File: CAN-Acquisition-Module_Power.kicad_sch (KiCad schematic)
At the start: 8 parts

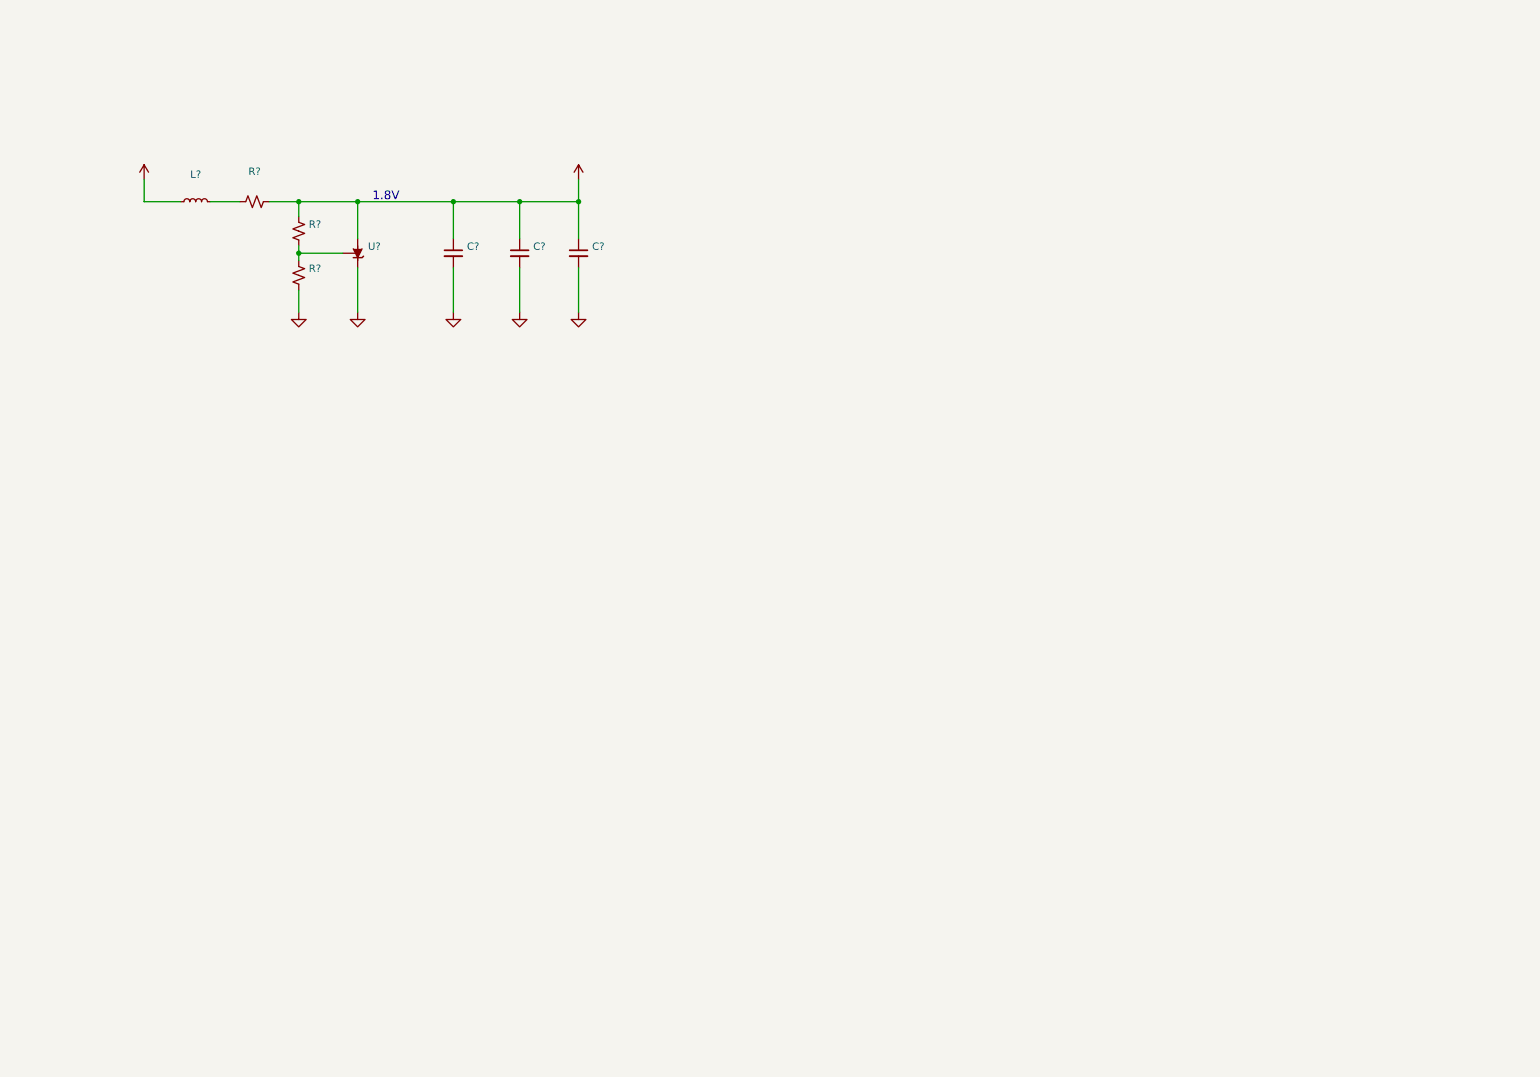
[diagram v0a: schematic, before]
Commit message: Added CAN page
also power section has advanced
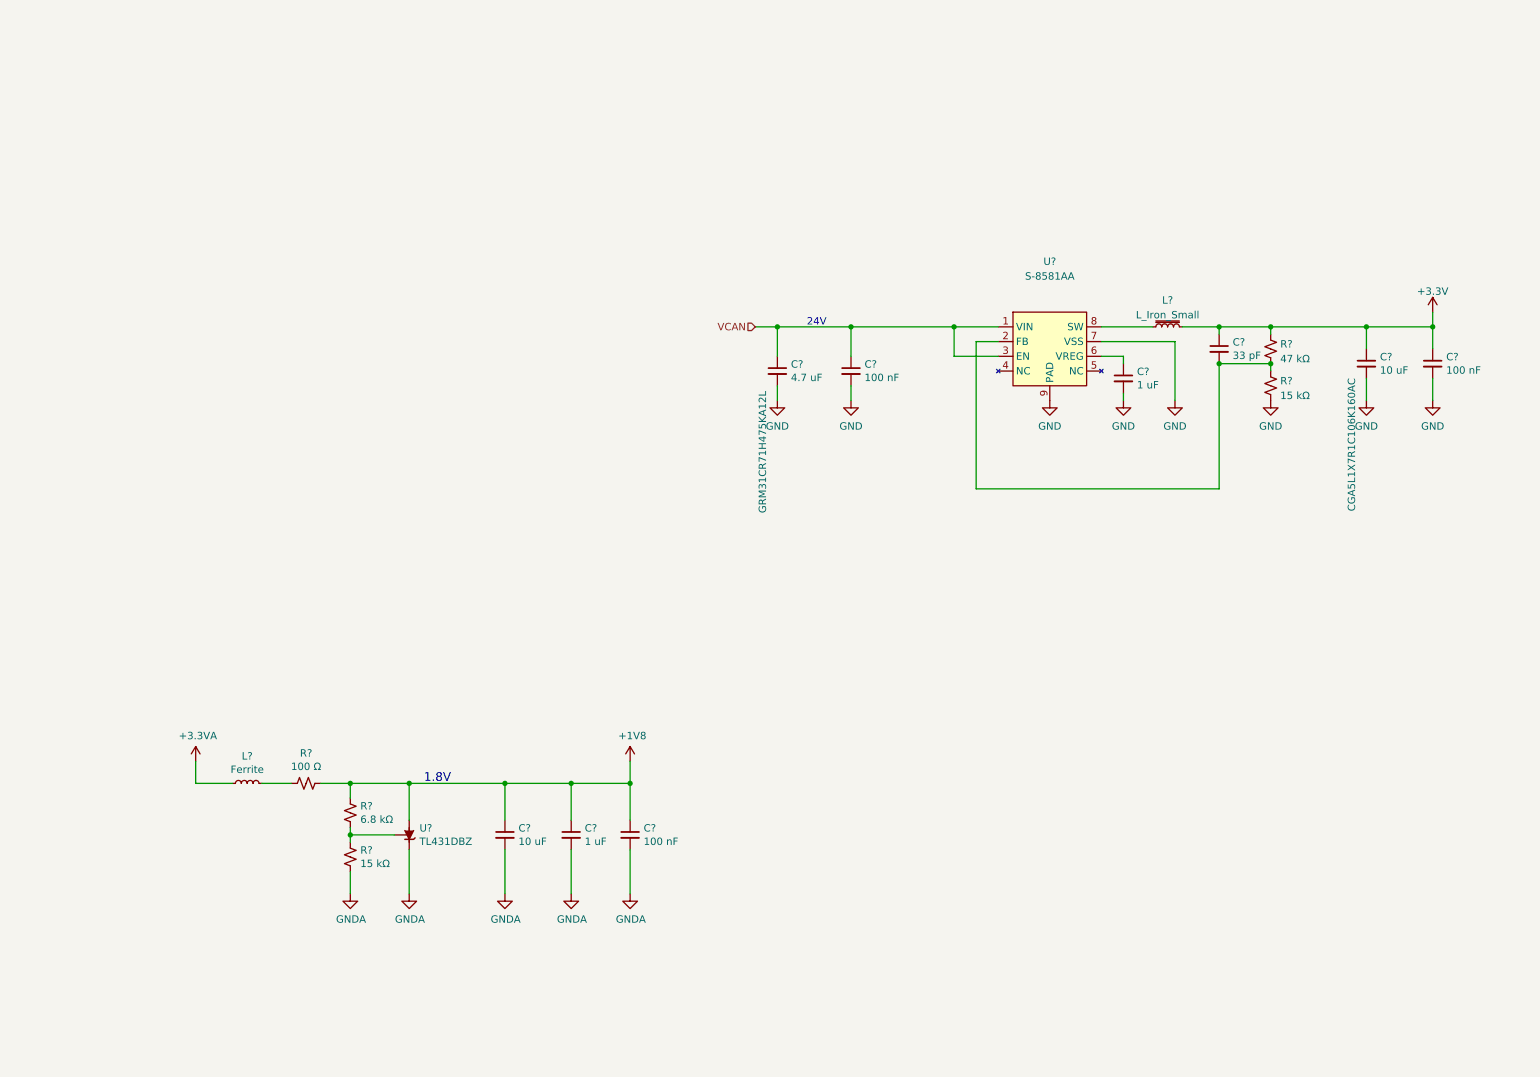
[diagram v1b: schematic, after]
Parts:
- added C?: 100 nF, Capacitor_SMD:C_0402_1005Metric, symbol Device:C_Small
- added C?: 100 nF, Capacitor_SMD:C_0603_1608Metric, symbol Device:C_Small
- added C?: 33 pF, Capacitor_SMD:C_0603_1608Metric, symbol Device:C_Small
- added C?: 10 uF, Capacitor_SMD:C_1206_3216Metric, symbol Device:C_Small
- added C?: 1 uF, Capacitor_SMD:C_0603_1608Metric, symbol Device:C_Small
- added C?: 4.7 uF, Capacitor_SMD:C_1206_3216Metric, symbol Device:C_Small
- added L?: L_Iron_Small, Inductor_SMD:L_1008_2520Metric, symbol Device:L_Iron_Small
- added R?: 15 kΩ, Resistor_SMD:R_0603_1608Metric, symbol Device:R_Small_US
- added R?: 47 kΩ, Resistor_SMD:R_0603_1608Metric, symbol Device:R_Small_US
- added U?: S-8581AA, CAN-Acquisition-Module:Ablic_HSTN-8-A, symbol CAN-Acquisition-Module:S-8581AA
- C?: value (none) -> 10 uF; footprint (none) -> Capacitor_SMD:C_1206_3216Metric
- C?: value (none) -> 1 uF; footprint (none) -> Capacitor_SMD:C_0603_1608Metric
- C?: value (none) -> 100 nF; footprint (none) -> Capacitor_SMD:C_0402_1005Metric
- L?: value (none) -> Ferrite; footprint (none) -> Inductor_SMD:L_0603_1608Metric
- R?: value (none) -> 6.8 kΩ; footprint (none) -> Resistor_SMD:R_0603_1608Metric
- R?: value (none) -> 15 kΩ; footprint (none) -> Resistor_SMD:R_0603_1608Metric
- R?: value (none) -> 100 Ω; footprint (none) -> Resistor_SMD:R_0805_2012Metric
- U?: value (none) -> TL431DBZ; footprint (none) -> Package_TO_SOT_SMD:SOT-23
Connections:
- new net: C?.2, R?.1, R?.2, U?.2 (FB)
- new net: C?.1, U?.6 (VREG)
- new net: L?.1, U?.8 (SW)
- new net +3V3: C?.1, C?.1, C?.1, L?.2, R?.1
- new net GND: C?.2, C?.2, C?.2, C?.2, C?.2, R?.2, U?.7 (VSS), U?.9 (PAD)
- new net VCAN: C?.1, C?.1, U?.1 (VIN), U?.3 (EN)
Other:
- note added: "24V"
- moved on the sheet: C?, L?, R?, U?

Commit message: Mid-day backup
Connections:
- net VCAN: no longer names the net of C?.1, C?.1, U?.1 (VIN), U?.3 (EN)
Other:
- note added: "5 to 24V"
- note removed: "24V"
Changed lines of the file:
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@@
   (junction (at 236.22 73.66) (diameter 0) (color 0 0 0 0)
-  )
-  (junction (at 151.13 67.31) (diameter 0) (color 0 0 0 0)
   )
   (junction (at 264.16 67.31) (diameter 0) (color 0 0 0 0)
@@
   )
   (wire (pts (xy 264.16 67.31) (xy 252.73 67.31))
-    (stroke (width 0) (type default) (color 0 0 0 0))
-  )
-  (wire (pts (xy 147.32 67.31) (xy 151.13 67.31))
     (stroke (width 0) (type default) (color 0 0 0 0))
   )
@@
     (stroke (width 0) (type default) (color 0 0 0 0))
   )
-  (text "24V" (at 156.21 67.31 0)
+  (text "5 to 24V" (at 156.21 67.31 0)
     (effects (font (size 1.27 1.27)) (justify left bottom))
   )
@@
     (effects (font (size 1.4986 1.4986)) (justify left bottom))
   )
-  (hierarchical_label "VCAN" (shape input) (at 147.32 67.31 180)
+  (hierarchical_label "V_CAN" (shape input) (at 88.9 67.31 180)
     (effects (font (size 1.27 1.27)) (justify right))
   )
+  (hierarchical_label "V_USB" (shape input) (at 88.9 38.1 180)
+    (effects (font (size 1.27 1.27)) (justify right))
+  )

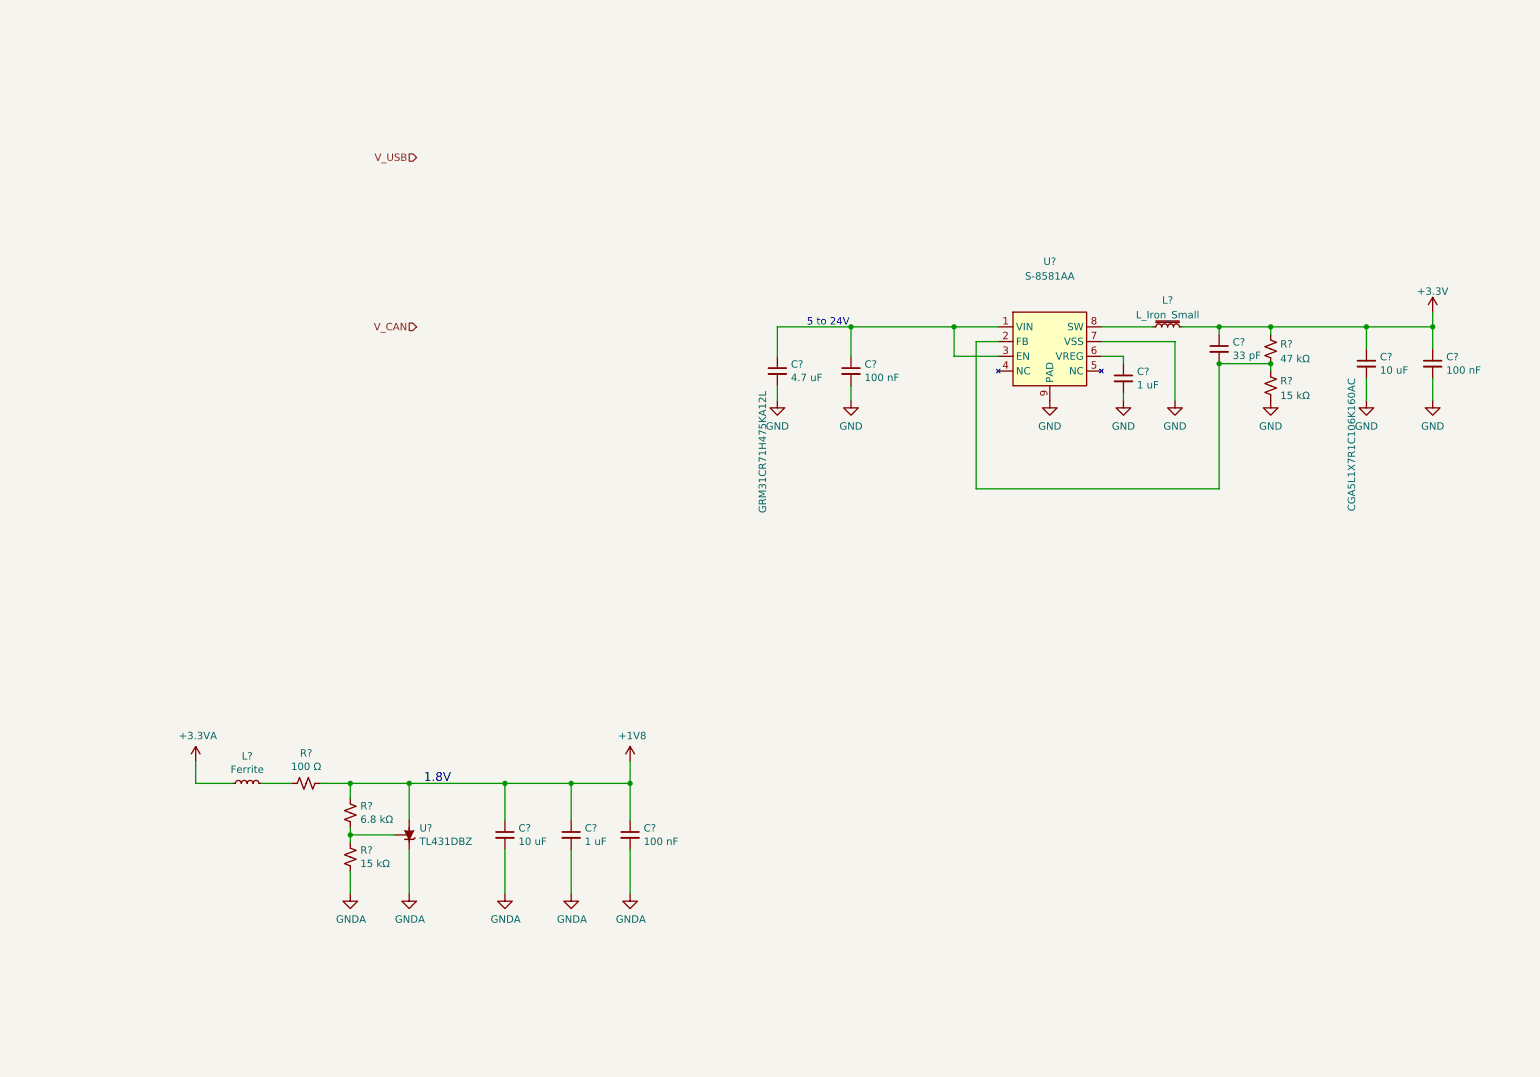
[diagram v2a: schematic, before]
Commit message: Advanced CAN section and "finished" power section
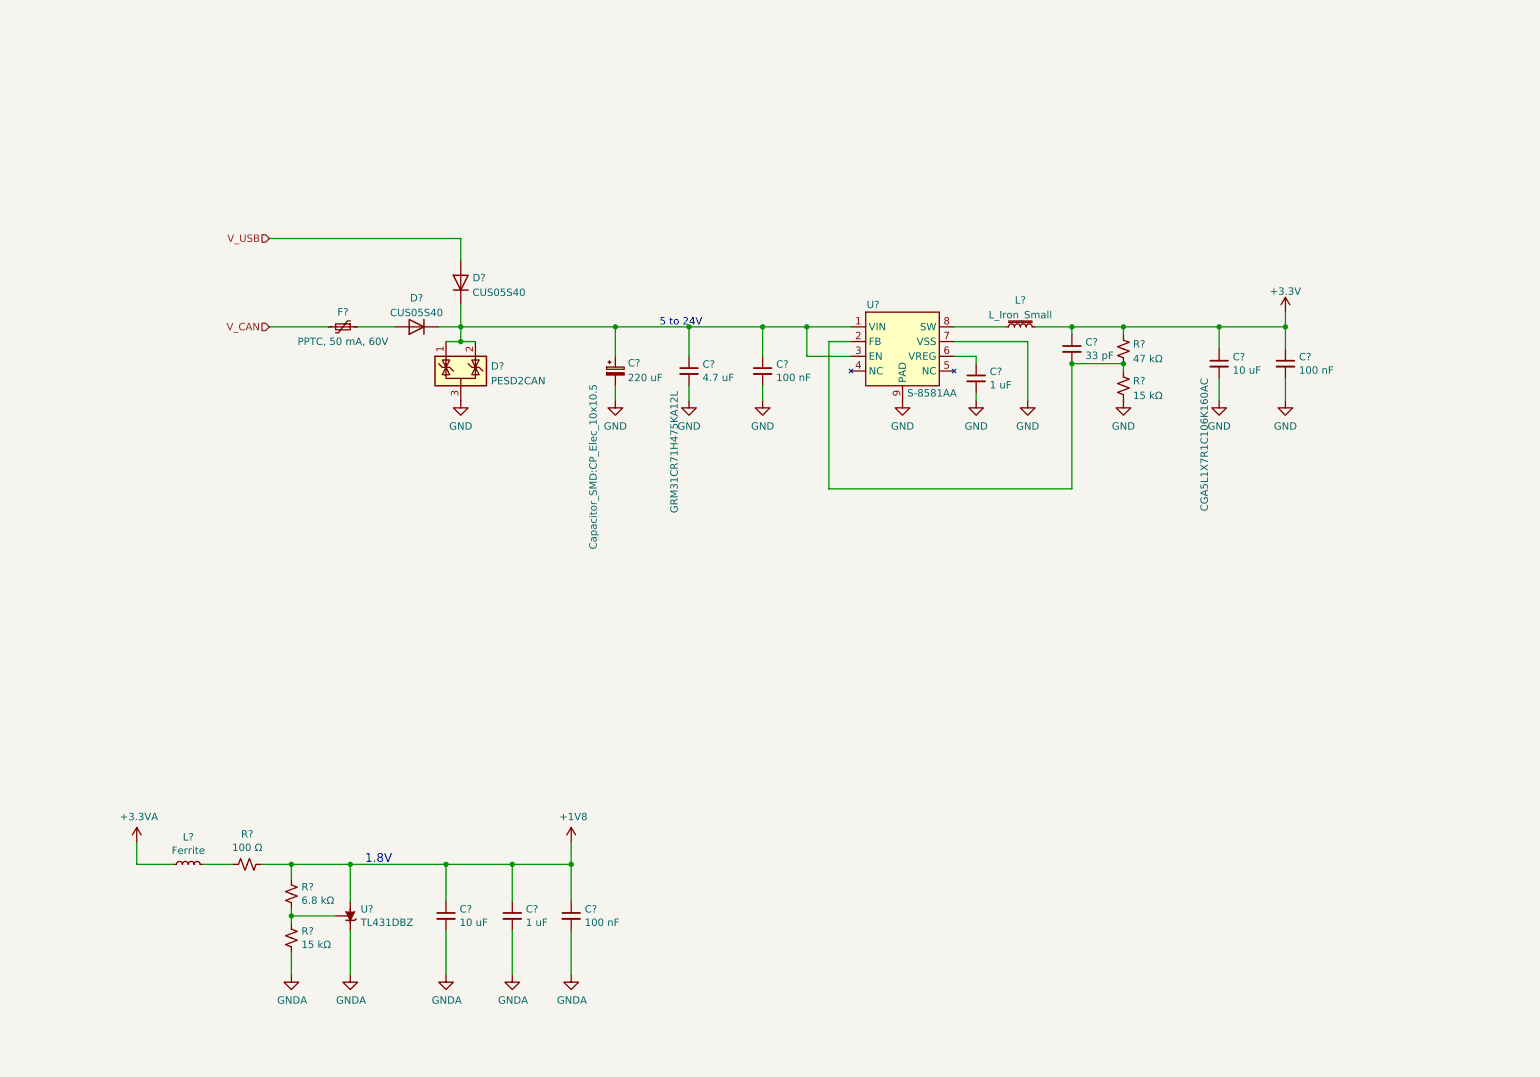
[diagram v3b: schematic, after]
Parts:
- added C?: 220 uF, Capacitor_SMD:CP_Elec_10x10.5, symbol Device:C_Polarized_Small
- added D?: PESD2CAN, Package_TO_SOT_SMD:SOT-23, symbol Power_Protection:NUP2105L
- added D? (x2): CUS05S40, CAN-Acquisition-Module:Toshiba_USC, symbol Device:D
- added F?: PPTC, 50 mA, 60V, Fuse:Fuse_1206_3216Metric, symbol Device:Polyfuse_Small
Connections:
- net GND: now also C?.2, D?.3 (A)
- net V_CAN: now also F?.2
- net V_USB: now also D?.2 (A)
- net at C?.1, C?.1, U?.1 (VIN)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: now also C?.1, D?.1 (K), D?.1 (K), D?.1 (K), D?.2 (K)
- new net: D?.2 (A), F?.1
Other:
- moved on the sheet: C?, L?, R?, U?

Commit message: Added stuff and cleanup
Added LED, Power outputs, additional descriptions
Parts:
- added C? (x3): 4.7 uF, Capacitor_SMD:C_1206_3216Metric, symbol Device:C_Small
- added C?: 100 nF, Capacitor_SMD:C_0603_1608Metric, symbol Device:C_Small
- added D?: CUS05S40, CAN-Acquisition-Module:Toshiba_USC, symbol Device:D
- added D? (x2): CM1213A-01SO, Package_TO_SOT_SMD:SOT-23, symbol Power_Protection:CM1213A-01SO
- added J?: Conn_01x02, Connector_PinHeader_2.54mm:PinHeader_1x02_P2.54mm_Vertical, symbol Connector_Generic:Conn_01x02
- added J?: Conn_01x04, Connector:FanPinHeader_1x04_P2.54mm_Vertical, symbol Connector_Generic:Conn_01x04
- added L?: 330 uF, Inductor_SMD:L_Bourns_SRN6045TA, symbol Device:L_Iron_Small
- added Q?: SI2318A, Package_TO_SOT_SMD:SOT-23, symbol Transistor_FET:2N7002K
- added R?: Ω, Resistor_SMD:R_0603_1608Metric, symbol Device:R_Small_US
- added R? (x3): 10 kΩ, Resistor_SMD:R_0603_1608Metric, symbol Device:R_Small_US
- F?: value PPTC, 50 mA, 60V -> PPTC, 50-500mA, 60V
- L?: value L_Iron_Small -> 4.7 uH; MPN (none) -> TFM252012ALVA4R7MTAA
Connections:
- net +3V3: now also D?.2 (VP), D?.2 (VP), R?.2
- net GND: now also C?.2, C?.2, C?.2, C?.2, D?.3 (VN), D?.3 (VN), J?.1 (Pin_1), Q?.2 (S)
- net at C?.1, C?.1, C?.1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: now also L?.2; no longer D?.1 (K), D?.1 (K), D?.1 (K), D?.2 (K)
- new net: D?.2 (A), J?.2 (Pin_2), Q?.3 (D)
- new net: J?.4 (Pin_4), R?.2
- new net: J?.3 (Pin_3), R?.2
- new net: Q?.1 (G), R?.2
- new net FAN_PWM_CTRL: D?.1 (CH1), R?.1
- new net FAN_TACH: D?.1 (CH1), R?.1, R?.1
- new net POWER_OUTPUT: R?.1
- new net VBUS: C?.1, C?.1, C?.1, C?.1, D?.1 (K), D?.1 (K), D?.1 (K), D?.1 (K), D?.2 (K), J?.1 (Pin_1), J?.2 (Pin_2), L?.1
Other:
- note added: "500 mA max."
- note added: "Analog"
- note added: "FAN"
- note added: "Power outputs"
- note added: "Use R? and short R? if TACH output is open collector"
- moved on the sheet: C?, D?, F?, L?, R?, U?

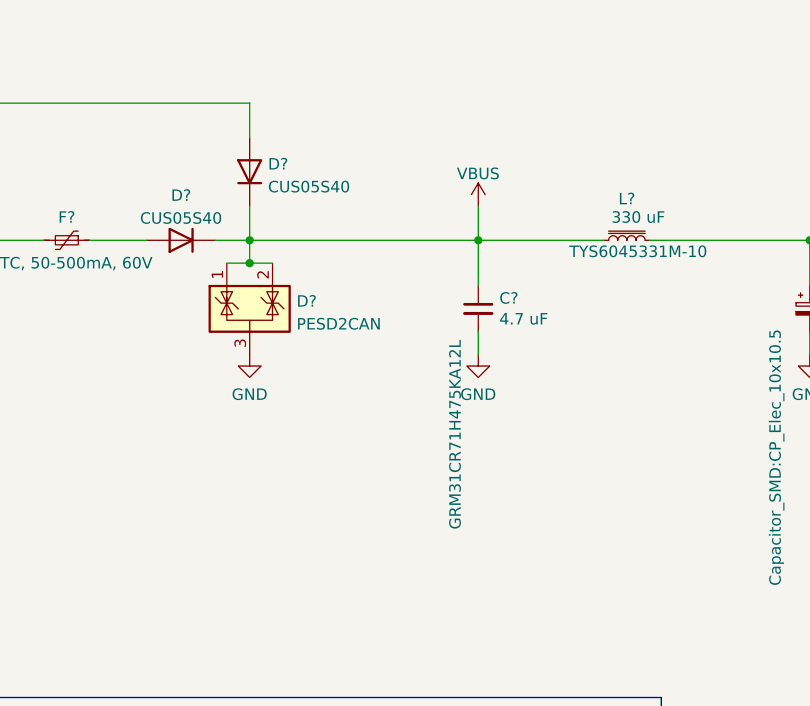
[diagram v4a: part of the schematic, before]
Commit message: Added analog and sensors sections
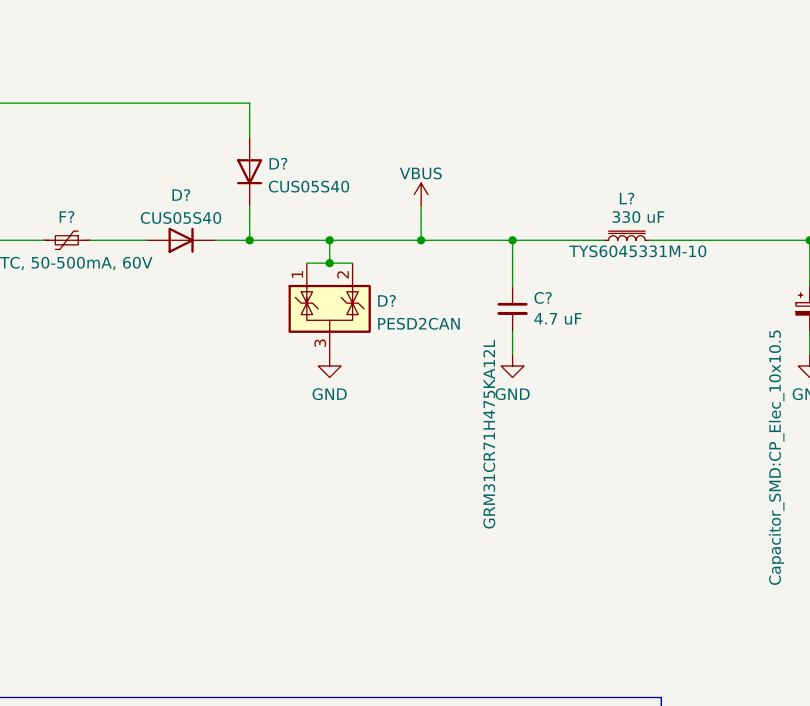
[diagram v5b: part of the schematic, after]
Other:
- company: (none) -> École de Technologie Supérieure - Laboratoire thermique et science du bâtiment (LTSB)
- title: (none) -> CANbus Acquisition Module
- moved on the sheet: C?, D?
